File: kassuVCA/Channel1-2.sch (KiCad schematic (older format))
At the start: 64 parts, among them Q401 MMBT3904, Q402 MBT3904DW1, Q403 MBT3904DW1, Q404 MMBT3904, U401 TL072, U402 TL072

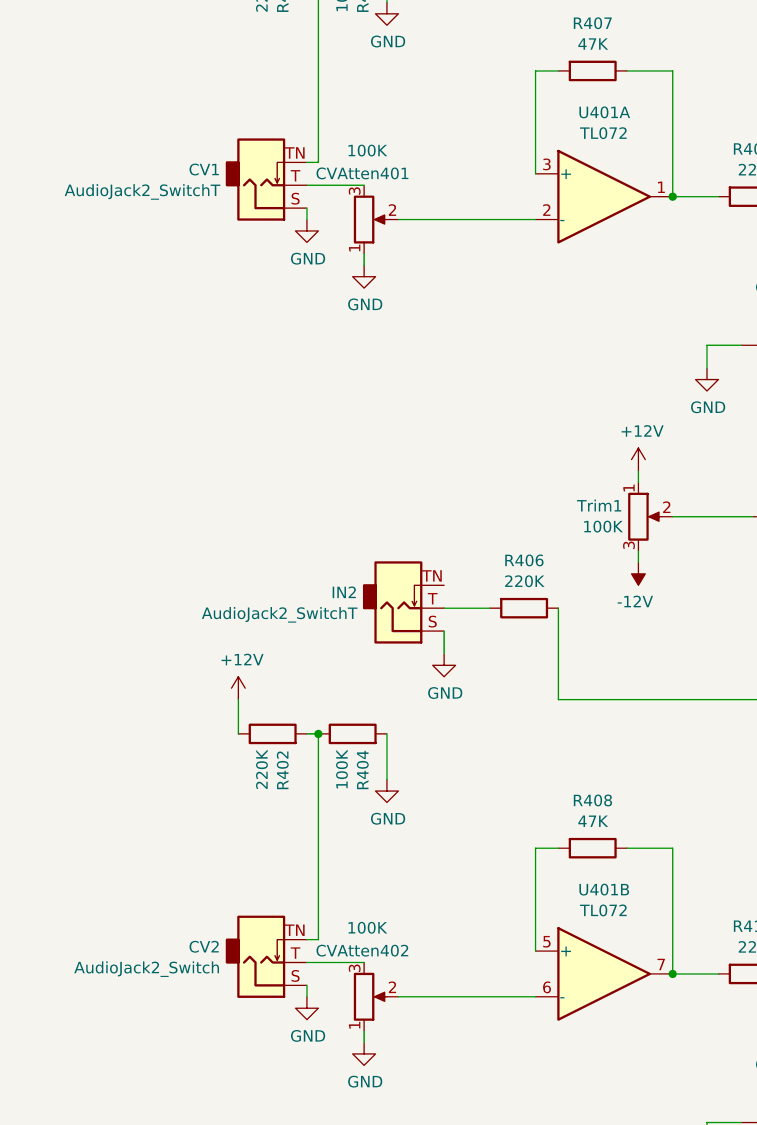
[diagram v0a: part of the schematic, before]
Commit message: mixer WIP, 8 channels, more or less
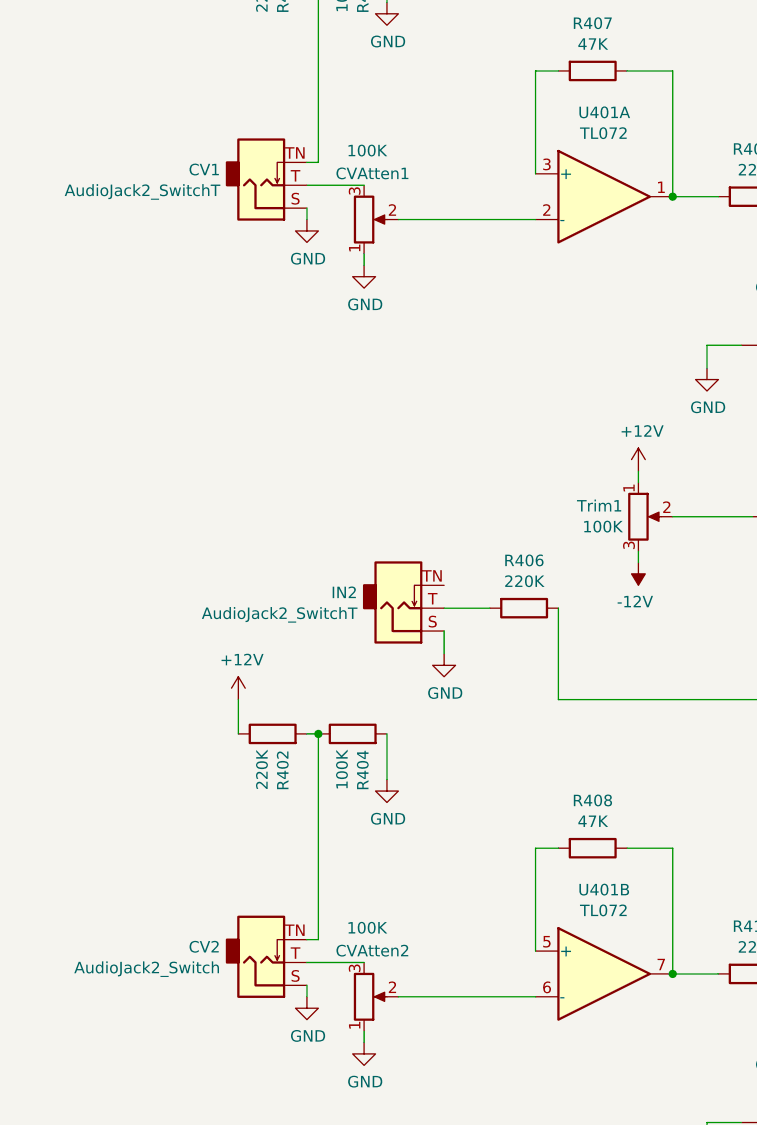
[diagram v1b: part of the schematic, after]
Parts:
- renumbered CVAtten401 to CVAtten1, CVAtten402 to CVAtten2
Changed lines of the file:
@@
 $Descr A4 11693 8268
 encoding utf-8
-Sheet 4 6
+Sheet 4 7
 Title ""
 Date ""
@@
 AR Path="/624C0657/624FE4CA/626359CC" Ref="CVAtten?"  Part="1"
 AR Path="/624C0657/624FE546/626359CC" Ref="CVAtten?"  Part="1"
-AR Path="/624C0657/62687518/626359CC" Ref="CVAtten401"  Part="1"
+AR Path="/624C0657/62687518/626359CC" Ref="CVAtten1"  Part="1"
 AR Path="/624C0657/628546A3/626359CC" Ref="CVAtten?"  Part="1"
-AR Path="/624C0657/62865DD7/626359CC" Ref="CVAtten501"  Part="1"
+AR Path="/624C0657/62865DD7/626359CC" Ref="CVAtten3"  Part="1"
 AR Path="/624C0657/625C0132/626359CC" Ref="CVAtten?"  Part="1"
-F 0 "CVAtten401" H 1450 2300 50  0000 R CNN
+F 0 "CVAtten1" H 1450 2300 50  0000 R CNN
 F 1 "100K" H 1350 2200 50  0000 R CNN
 F 2 "Potentiometer_THT:Potentiometer_Alps_RK09K_Single_Vertical" H 1250 2500 50  0001 C CNN
@@
 AR Path="/624C0657/624FE4CA/626349E7" Ref="CVAtten?"  Part="1"
 AR Path="/624C0657/624FE546/626349E7" Ref="CVAtten?"  Part="1"
-AR Path="/624C0657/62687518/626349E7" Ref="CVAtten402"  Part="1"
+AR Path="/624C0657/62687518/626349E7" Ref="CVAtten2"  Part="1"
 AR Path="/624C0657/628546A3/626349E7" Ref="CVAtten?"  Part="1"
-AR Path="/624C0657/62865DD7/626349E7" Ref="CVAtten502"  Part="1"
+AR Path="/624C0657/62865DD7/626349E7" Ref="CVAtten4"  Part="1"
 AR Path="/624C0657/625C0132/626349E7" Ref="CVAtten?"  Part="1"
-F 0 "CVAtten402" H 1450 5700 50  0000 R CNN
+F 0 "CVAtten2" H 1450 5700 50  0000 R CNN
 F 1 "100K" H 1350 5600 50  0000 R CNN
 F 2 "Potentiometer_THT:Potentiometer_Alps_RK09K_Single_Vertical" H 1250 5900 50  0001 C CNN
